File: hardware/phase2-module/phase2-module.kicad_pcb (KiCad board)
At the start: 4 copper layers, 130 x 90 mm, 180 parts, among them J1 XT60PW-M SLOT PWR, J2 SWD, J3 UART, J4 XT60PW-M OUTPUT, J5 SLOT SIGNALS, J6 FAN, Q1 CSD18540Q5B, Q10 CSD18540Q5B, Q11 CSD18540Q5B, Q12 CSD18540Q5B, Q13 CSD18540Q5B, Q14 CSD19536KTT, Q2 CSD18540Q5B, Q3 CSD18540Q5B, Q4 CSD18540Q5B, Q5 2N7002, Q6 2N7002, Q7 2N7002, Q8 2N7002, Q9 2N7002, U1 DAC80502DRXT, U10 STM32G431CBT6, U11 TCAN1042HGV, U12 LM5069MM-2, U13 TS5A3166, U2 OPA2333, U3 LM5143RHAR, U4 INA240A3, U5 INA228, U6 LTC7004, U7 TLV7011DCK, U8 LMR36015AQRNXRQ1, U9 NCP1117-3.3, Y1 8MHz

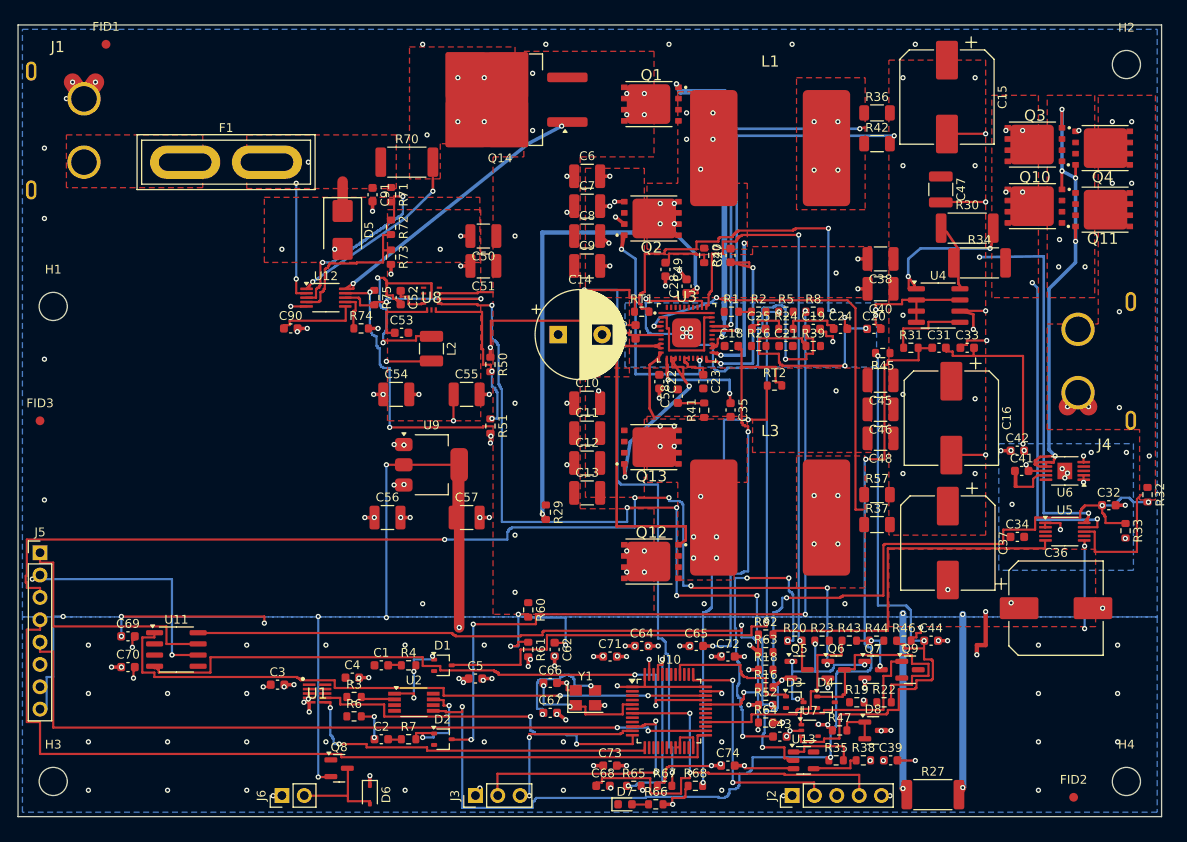
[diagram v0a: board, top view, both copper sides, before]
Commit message: Phase-2 board back to the clean pass-1 copper baseline (0 copper DRC)
Regenerated deterministically (gen_board.py + route_board.py) so the
tracked board is again the state HANDOVER intends to carry: placement,
pours, In2 patches, all pass-1 hand routes -- 0 clearance, 0 dangling,
0 shorts; 240 unconnected = the signal nets, untouched by any router.

This supersedes the autoroute output that 3da24a7 committed by accident
(88 unconnected but 4 clearance errors + 2 dangling slivers, from the
pre-fix router). Router output stays out of the tree until a run
converges; every intermediate is reproducible from the two generators.

Also ignores transient layout artifacts: tools/logs/ (freerouting) and
the KiCad 3D-model checker's *_missing3Dmodels.txt drops.

Co-Authored-By: Claude Fable 5 <noreply@anthropic.com>
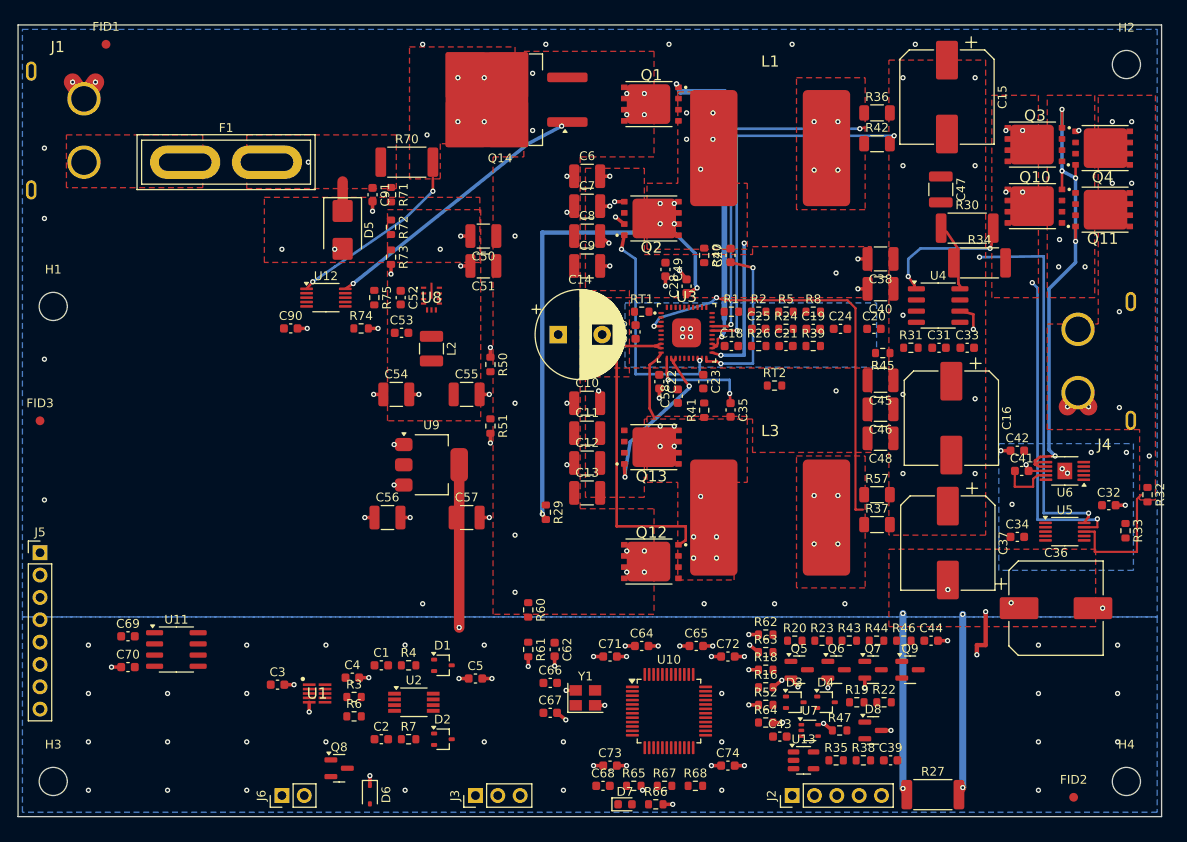
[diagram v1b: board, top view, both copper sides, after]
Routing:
- net AGND: track 197.8 -> 26.9 mm, vias 101 -> 63
- net I_MEAS: track 123.6 -> 0.00 mm, vias 3 -> 0
- net HW_EN: track 123.6 -> 0.00 mm, vias 6 -> 0
- net 5V0: track 113.5 -> 12.0 mm, vias 29 -> 9
- net SLOT_ID0: track 96.8 -> 0.00 mm
- net EAI_INJ: track 89.2 -> 0.00 mm, vias 4 -> 0
- net AUX_PG: track 86.9 -> 0.00 mm, vias 6 -> 0
- net SLOT_ID1: track 85.8 -> 0.00 mm, vias 2 -> 0
- net CAN_STB: track 85.4 -> 0.00 mm, vias 3 -> 0
- net V_MEAS: track 83.5 -> 0.00 mm, vias 4 -> 0
- net 3V3: track 109.8 -> 31.9 mm, vias 25 -> 13
- net EAV_INJ: track 77.3 -> 0.00 mm, vias 2 -> 0
- net NTC_FET: track 74.6 -> 0.00 mm, vias 2 -> 0
- net CAN_TX: track 72.5 -> 0.00 mm, vias 2 -> 0
- net CAN_RX: track 71.3 -> 0.00 mm, vias 2 -> 0
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
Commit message: Phase-2 board: autoroute + silk pass — 240 -> 83 unconnected, 0 copper DRC
Full deterministic pipeline (gen_board -> route_board -> autoroute ->
silk_refs) with the rebuilt router:

  unconnected   240 -> 83      (164 nets routed, 69 escapes refused)
  clearance       0            (stays clean: no shorts, no dangling)
  silk          154 -> 11      (160/180 refdes placed clean, 20 best-effort)
  DRC total     334 -> 191     (180 = the known-benign lib bookkeeping)

The 83 remaining split as ~35 items on plane nets (AGND 16, 5V0 9, PGND 7,
3V3 3 — pour-fragment stubs, a few vias each) and ~48 real signal escapes
clustered at U3's control pins and U10's QFN, which is where a grid maze
router runs out of room. KiCad's interactive push-and-shove is the right
tool for those; the per-net list is in HANDOVER.

PS-002 stitching removed from STITCH rather than left broken: the two
coordinates added earlier never placed (too_close rejected them), and the
underlying reason matters — island geometry depends on the FINISHED
copper, so islands move as routing carves the pours. It is a final pass,
not a route_board constant. Documented in place.

Freerouting was ruled out with evidence, not vibes: with zones it throws
StackOverflowError in PolylineTrace.combine (this is what the KiCad
plugin hits too — it exports zones); zone-free it clears that crash but
a jstack thread dump caught it spinning in PolylineTrace.normalize ->
ShapeSearchTree.overlapping_tree_entries for 2 hours with no output.

Co-Authored-By: Claude Fable 5 <noreply@anthropic.com>
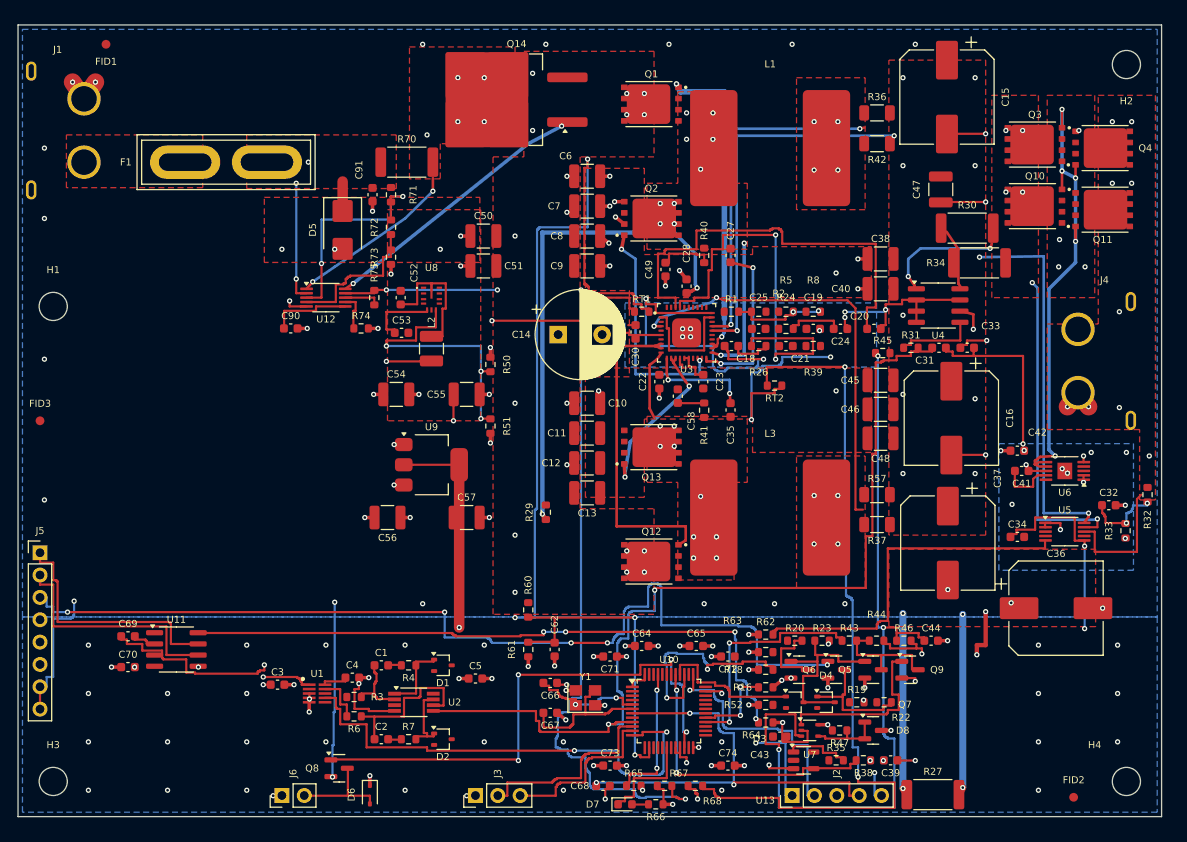
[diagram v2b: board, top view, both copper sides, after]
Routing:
- net AGND: track 26.9 -> 229.4 mm, vias 63 -> 89
- net HW_EN: track 0.00 -> 111.0 mm, vias 0 -> 5
- net I_MEAS: track 0.00 -> 107.9 mm, vias 0 -> 2
- net OVP_DIV: track 0.00 -> 92.7 mm, vias 0 -> 3
- net NTC_IND: track 0.00 -> 91.0 mm, vias 0 -> 2
- net NTC_FET: track 0.00 -> 87.3 mm, vias 0 -> 2
- net CAN_STB: track 0.00 -> 75.1 mm, vias 0 -> 4
- net FAN_PWM: track 0.00 -> 62.4 mm, vias 0 -> 4
- net 3V3: track 31.9 -> 89.9 mm, vias 13 -> 22
- net DAC_NSYNC: track 0.00 -> 56.7 mm, vias 0 -> 2
- net 5V0: track 12.0 -> 68.7 mm, vias 9 -> 17
- net PGND: track 61.1 -> 115.8 mm, vias 51 -> 58
- net NRST: track 0.00 -> 51.7 mm, vias 0 -> 3
- net PS_DITH: track 0.00 -> 48.2 mm
- net PS_RT: track 0.00 -> 47.8 mm, vias 0 -> 2
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
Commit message: Backplane fab-ready; DRC "benign bookkeeping" was two real bugs
The lib_footprint_issues class everyone has been waving through (39
backplane, 180 phase-2, 144 phase-1) was never one thing, and neither
half was harmless bookkeeping:

 1. The board generators add footprints by name only, leaving the FPID
    library nickname empty. common/fix_fpids.py resolves each item name
    against the project library first, then the system libraries, and
    writes the nickname back (363 resolved across three boards, none
    guessed — unresolved names are reported, never invented).
 2. KiCad's global fp-lib-table expands ${KICAD7_FOOTPRINT_DIR}, which
    only the GUI sets. Headless DRC could not expand a single library
    URI, so every footprint came back "not found in library". Every
    run_drc.py now sets it before importing pcbnew.

Both mattered beyond noise: with the libraries unresolved, KiCad cannot
diff a board footprint against its library, so silent land-pattern drift
would pass unnoticed — and this project already caught one such bug in
LM5143 by hand.

    phase3-backplane   40 -> 0 violations, 0 unconnected
    phase2-module     191 -> 11 (silk only), 83 unconnected
    phase1-module     247 -> 75 (silk only)

phase3-backplane is now FAB-READY: silk reflowed (39/39 refs clean), no
plane islands, gerbers + drills plotted and cross-checked — Edge_Cuts
exactly 330.00 x 100.00 mm, drills 2x6.4mm (M6 entry lugs), 16x2.8mm
(8 slots x 2 XT60 pins), 6x3.2mm (M3), 86x1.0mm, 61x0.4mm.

New shared tooling in hardware/common (was phase-2-only, now serves every
board): layout_qa.py (silk reflow, PS-002 islands, gerber/drill plot with
the layer set read from the board) and finish_board.py as its CLI.

Correction: phase-1 is 187 unconnected, not the 33 in HANDOVER — that
figure came from an autoroute run that was never committed, and its
gitignored drc-report.txt kept showing the stale number. Verified against
the committed board.

Co-Authored-By: Claude Fable 5 <noreply@anth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
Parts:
- C1, C18, C19, C2, C20, C21, C22, C23, C24, C25, C27, C28, C3, C30, C31, C32, C33, C34, C35, C39, C4, C41, C42, C43, C44, C49, C5, C52, C53, C58, C62, C64, C65, C66, C67, C68, C69, C70, C71, C72, C73, C74, C90, C91: footprint C_0603_1608Metric -> Capacitor_SMD:C_0603_1608Metric
- C10, C11, C12, C13, C38, C40, C45, C46, C47, C48, C50, C51, C54, C55, C56, C57, C6, C7, C8, C9: footprint C_1210_3225Metric -> Capacitor_SMD:C_1210_3225Metric
- C14: footprint CP_Radial_D10.0mm_P5.00mm -> Capacitor_THT:CP_Radial_D10.0mm_P5.00mm
- C15, C16, C36, C37: footprint CP_Elec_10x10.5 -> Capacitor_SMD:CP_Elec_10x10.5
- D1, D2, D3, D4: footprint SOT-323_SC-70 -> Package_TO_SOT_SMD:SOT-323_SC-70
- D5: footprint D_SMB -> Diode_SMD:D_SMB
- D6: footprint D_SOD-323 -> Diode_SMD:D_SOD-323
- D7: footprint LED_0603_1608Metric -> LED_SMD:LED_0603_1608Metric
- D8, Q5, Q6, Q7, Q8, Q9: footprint SOT-23 -> Package_TO_SOT_SMD:SOT-23
- F1: footprint Fuse_Blade_ATO_directSolder -> Fuse:Fuse_Blade_ATO_directSolder
- FID1, FID2, FID3: footprint Fiducial_1mm_Mask2mm -> Fiducial:Fiducial_1mm_Mask2mm
- H1, H2, H3, H4: footprint MountingHole_3.2mm_M3 -> MountingHole:MountingHole_3.2mm_M3
- J1, J4: footprint XT60PW-M -> labbench:XT60PW-M
- J2: footprint PinHeader_1x05_P2.54mm_Vertical -> Connector_PinHeader_2.54mm:PinHeader_1x05_P2.54mm_Vertical
- J3: footprint PinHeader_1x03_P2.54mm_Vertical -> Connector_PinHeader_2.54mm:PinHeader_1x03_P2.54mm_Vertical
- J5: footprint PinHeader_1x08_P2.54mm_Vertical -> Connector_PinHeader_2.54mm:PinHeader_1x08_P2.54mm_Vertical
- J6: footprint PinHeader_1x02_P2.54mm_Vertical -> Connector_PinHeader_2.54mm:PinHeader_1x02_P2.54mm_Vertical
- L1, L3: footprint L_1707_XAL1510 -> labbench:L_1707_XAL1510
- L2: footprint L_1210_3225Metric -> Inductor_SMD:L_1210_3225Metric
- NT1: footprint NetTie-2_SMD_Pad0.5mm -> NetTie:NetTie-2_SMD_Pad0.5mm
- Q1, Q10, Q11, Q12, Q13, Q2, Q3, Q4: footprint PowerFET_SON5x6_GDS -> labbench:PowerFET_SON5x6_GDS
- Q14: footprint TO-263-2 -> Package_TO_SOT_SMD:TO-263-2
- R1, R16, R18, R19, R2, R20, R22, R23, R24, R26, R29, R3, R31, R32, R33, R35, R38, R39, R4, R40, R41, R43, R44, R45, R46, R47, R5, R50, R51, R52, R6, R60, R61, R62, R63, R64, R65, R66, R67, R68, R7, R71, R72, R73, R74, R75, R8, RT1, RT2: footprint R_0603_1608Metric -> Resistor_SMD:R_0603_1608Metric
- R27, R30, R34, R70: footprint R_2512_6332Metric -> Resistor_SMD:R_2512_6332Metric
- R36, R37, R42, R57: footprint R_1206_3216Metric -> Resistor_SMD:R_1206_3216Metric
- U1: footprint DAC80502_DRX_WSON-10 -> labbench:DAC80502_DRX_WSON-10
- U10: footprint LQFP-48_7x7mm_P0.5mm -> Package_QFP:LQFP-48_7x7mm_P0.5mm
- U11, U4: footprint SOIC-8_3.9x4.9mm_P1.27mm -> Package_SO:SOIC-8_3.9x4.9mm_P1.27mm
- U12, U5: footprint VSSOP-10_3x3mm_P0.5mm -> Package_SO:VSSOP-10_3x3mm_P0.5mm
- U13: footprint SOT-23-5 -> Package_TO_SOT_SMD:SOT-23-5
- U2: footprint VSSOP-8_3.0x3.0mm_P0.65mm -> Package_SO:VSSOP-8_3.0x3.0mm_P0.65mm
- U3: footprint LM5143_RHA0040P -> labbench:LM5143_RHA0040P
- U6: footprint MSOP-10-1EP_3x3mm_P0.5mm_EP1.68x1.88mm -> Package_SO:MSOP-10-1EP_3x3mm_P0.5mm_EP1.68x1.88mm
- U7: footprint SOT-353_SC-70-5 -> Package_TO_SOT_SMD:SOT-353_SC-70-5
- U8: footprint LMR36015_RNX_VQFN-HR-12 -> labbench:LMR36015_RNX_VQFN-HR-12
- U9: footprint SOT-223-3_TabPin2 -> Package_TO_SOT_SMD:SOT-223-3_TabPin2
- Y1: footprint Crystal_SMD_3225-4Pin_3.2x2.5mm -> Crystal:Crystal_SMD_3225-4Pin_3.2x2.5mm

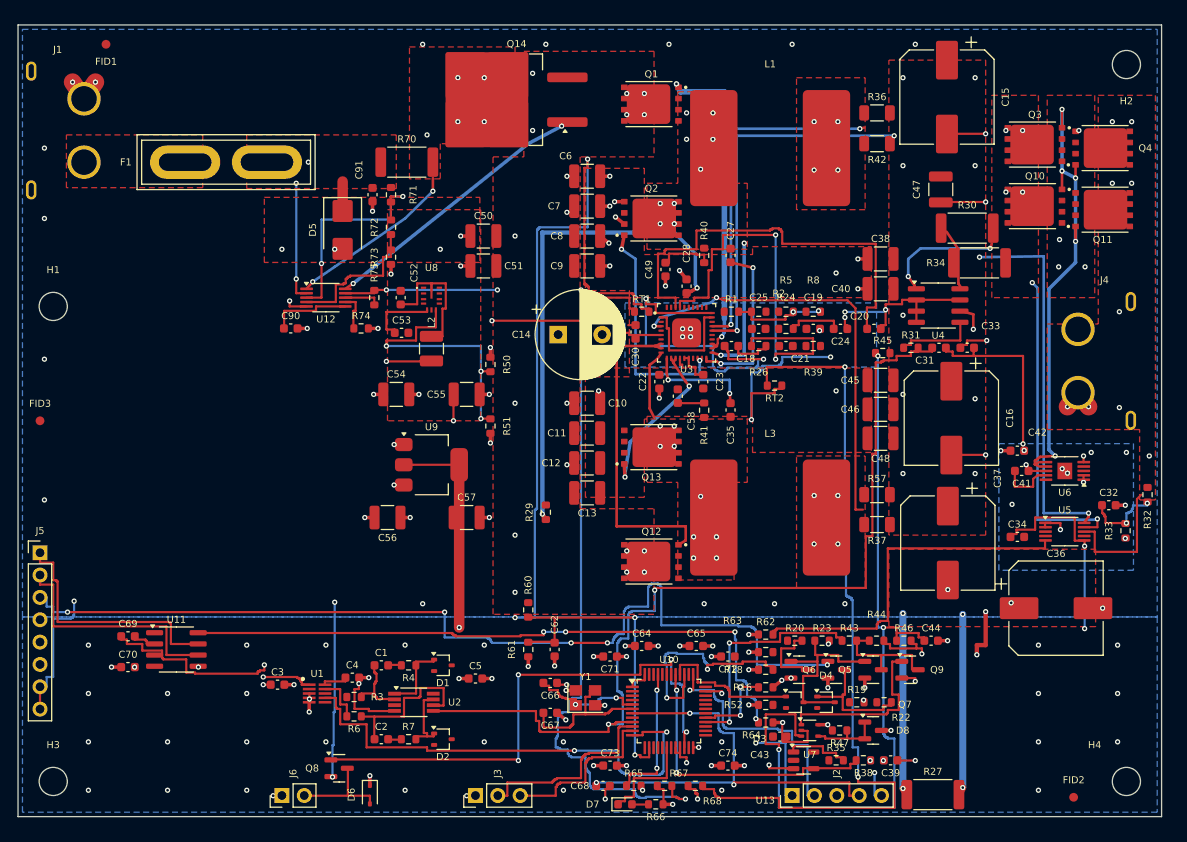
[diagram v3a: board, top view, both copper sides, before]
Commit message: phase2: finish routing (0 unconnected, 0 DRC errors) and generate fab outputs
Freerouting plus finish_routes closed all but EAI_INJ; CAN_TX's router
copper fenced the MCU area, so it was stripped and re-routed after
EAI_INJ. Silk, planes (PS-002 clear), DRC, gerbers/drill zip and the
JLCPCB CPL are regenerated. Adds tools/README.md and strip_routes.py,
and updates HANDOVER.

Co-Authored-By: Claude Opus 5.5 (1M context) <noreply@anthropic.com>
Claude-Session: https://claude.ai/code/session_01CT7ZUC1wFK39SLj4Qnh9qy
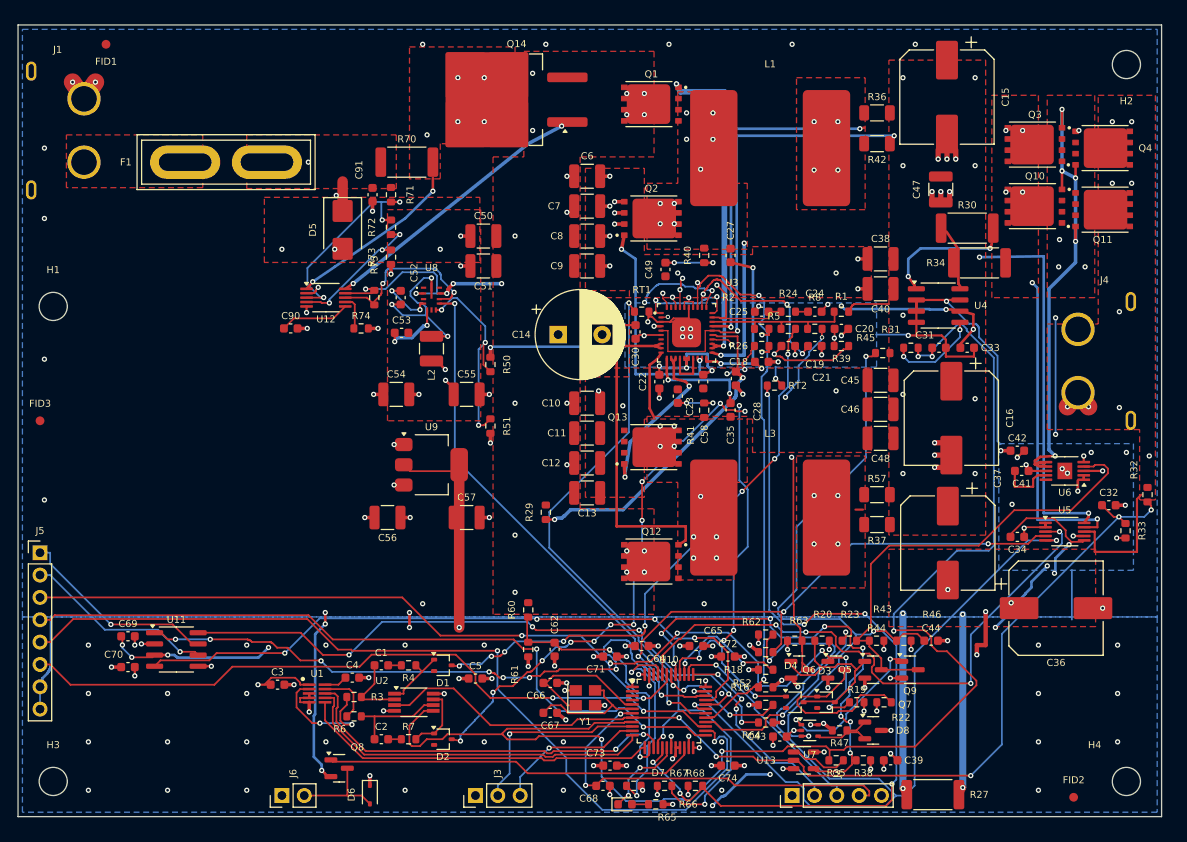
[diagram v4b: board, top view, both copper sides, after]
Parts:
- moved R1 12.5 mm to (113.6, 52.6), turned to 180 degrees
- moved C28 11.9 mm to (101.6, 60.2), turned to -90 degrees
- moved C18 3.88 mm to (104.5, 58.3)
- moved C20 3.70 mm to (113.6, 54.5)
- moved C24 3.51 mm to (110.6, 52.6)
- moved R39 3.20 mm to (113.6, 56.5)
- moved C25 1.98 mm to (104.5, 52.6), turned to 180 degrees
- moved R2 1.98 mm to (104.5, 54.5)
- moved R24 1.97 mm to (107.6, 52.6)
- moved R5 1.97 mm to (107.6, 54.5), turned to 180 degrees
- moved C19 1.96 mm to (110.6, 56.5)
- moved R8 1.96 mm to (110.6, 54.5), turned to 180 degrees
- moved R26 0.34 mm to (104.5, 56.5)
- moved C21 0.26 mm to (107.6, 56.5)
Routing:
- net V_MEAS: track 9.63 -> 116.5 mm, vias 2 -> 5
- net SLOT_ID1: track 0.00 -> 101.0 mm, vias 0 -> 2
- net AGND: track 229.4 -> 132.2 mm, vias 89 -> 100
- net SLOT_ID0: track 0.00 -> 84.5 mm, vias 0 -> 2
- net SLOT_ID2: track 0.00 -> 82.0 mm, vias 0 -> 2
- net CAN_RX: track 0.00 -> 76.1 mm, vias 0 -> 4
- net EAI_INJ: track 0.00 -> 74.8 mm, vias 0 -> 13
- net CAN_TX: track 0.00 -> 74.0 mm, vias 0 -> 8
- net 5V0: track 68.7 -> 139.7 mm, vias 17 -> 33
- net AUX_PG: track 0.00 -> 70.5 mm, vias 0 -> 4
- net I2C_SCL: track 41.6 -> 111.1 mm, vias 0 -> 3
- net I2C_SDA: track 0.00 -> 69.3 mm, vias 0 -> 4
- net INA_ALERT: track 0.00 -> 66.5 mm, vias 0 -> 4
- net EAV_INJ: track 0.00 -> 64.3 mm, vias 0 -> 8
- net I_MEAS: track 107.9 -> 164.8 mm, vias 2 -> 5
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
